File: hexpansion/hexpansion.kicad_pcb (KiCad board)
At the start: 2 copper layers, 32 x 36.6 mm, 17 parts, among them J1 Hexpansion-Connector, J2 Conn_01x08_Pin, U1 24LC00, U2 ATSHA204A-SSHDA

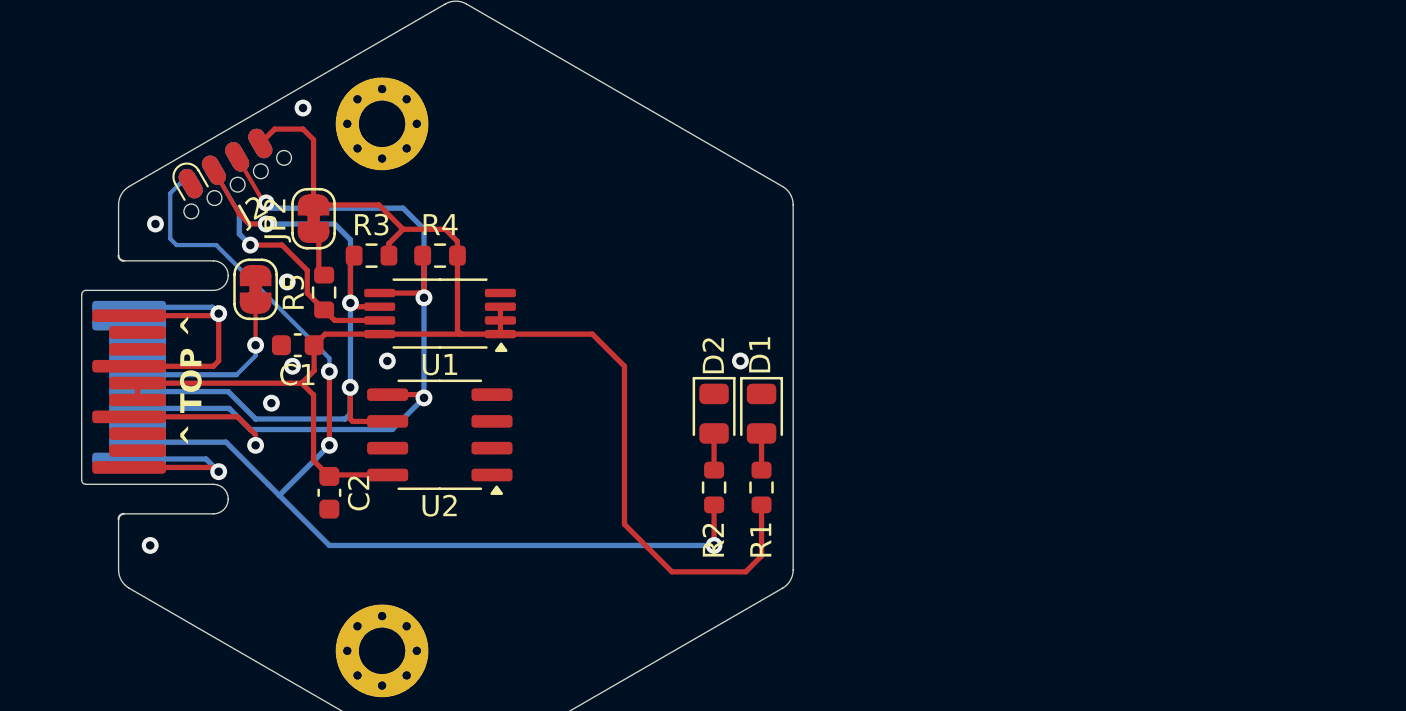
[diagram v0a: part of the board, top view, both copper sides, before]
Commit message: Update hexpansion design
Adds TVS diode
Removes seperate programming connector
tidy up PCB layout
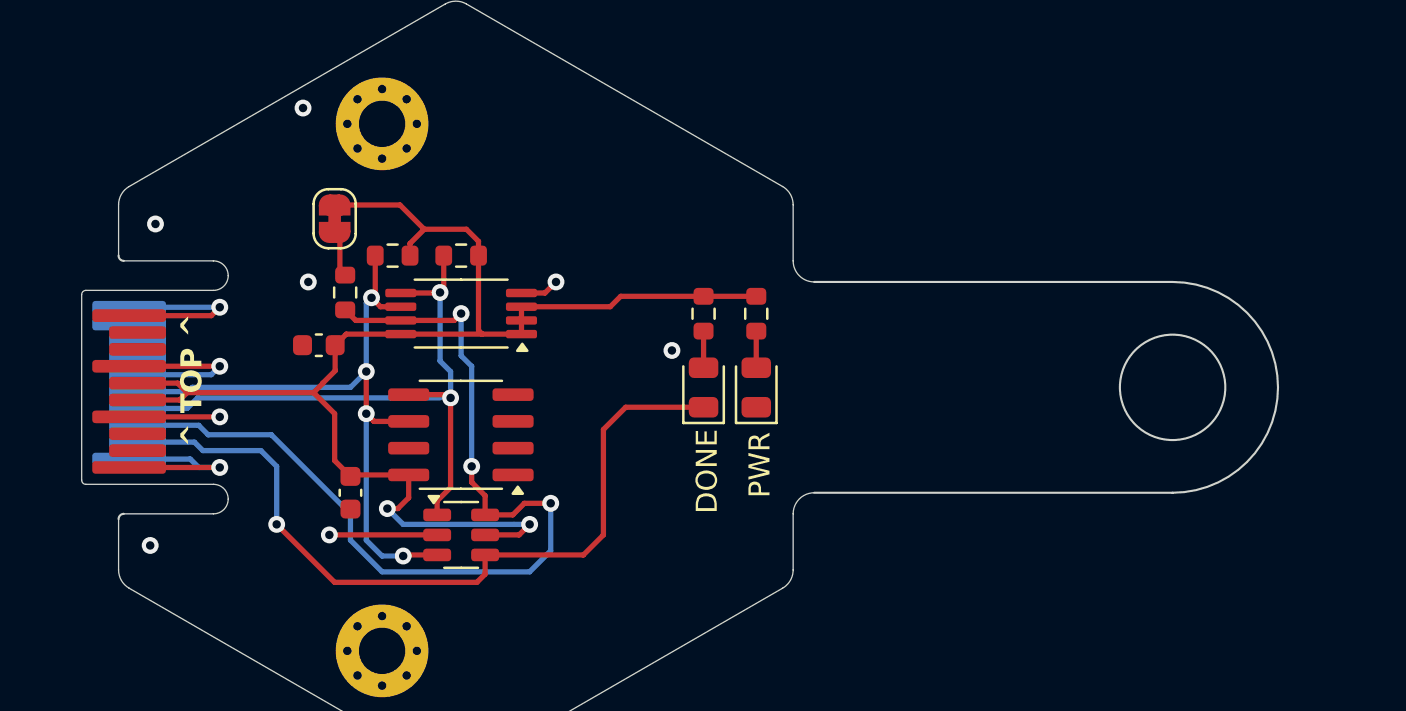
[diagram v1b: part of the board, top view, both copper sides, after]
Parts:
- removed J2: Conn_01x08_Pin, hexpansion:SOIC_clipProgSmall
- removed JP1: SolderJumper_2_Bridged, Jumper:SolderJumper-2_P1.3mm_Bridged_RoundedPad1.0x1.5mm
- added U3: WE-TVS-824015043, Package_TO_SOT_SMD:SOT-23-6, F.Cu at (116.2, 107.0)
- moved R2 8.26 mm to (127.8, 96.5), turned to -90 degrees
- moved R1 8.25 mm to (130.2, 96.5), turned to -90 degrees
- moved D2 1.34 mm to (127.8, 100.0), turned to 90 degrees
- moved D1 1.27 mm to (130.2, 100.0), turned to 90 degrees
- moved C1 1.00 mm to (109.5, 98.0)
- moved C2 1.00 mm to (111.0, 105.0)
- moved JP2 1.00 mm to (110.2, 92.0)
- moved R3 1.00 mm to (113.0, 93.8)
- moved R4 1.00 mm to (116.2, 93.8)
- moved R5 1.00 mm to (110.8, 95.5)
- moved U1 1.00 mm to (116.2, 96.5)
- moved U2 1.00 mm to (116.2, 102.2)
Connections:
- D2 pad 1: GND -> /LED_STATUS
- J1 pad 3: unconnected-(J1-LS_B-Pad3) -> /EEPROM_WP
- J1 pad 6: /HEXP_DET -> GND
- R2 pad 1: /LED_STATUS -> +3V3
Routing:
- net /EEPROM_WP: track 12.3 -> 45.1 mm, vias 1 -> 3
- net /LED_STATUS: track 52.0 -> 38.1 mm, vias 3 -> 1
- net /HEXP_DET: track 8.47 -> 0.00 mm, vias 1 -> 0
- net /SDA: track 38.9 -> 31.3 mm, vias 3 -> 2
- net GND: track 30.5 -> 37.2 mm
- net +3V3: track 72.6 -> 68.1 mm, vias 0 -> 2
- net /SCL: track 34.2 -> 32.3 mm, vias 3 -> 4
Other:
- board size 32 x 36.6 mm -> 55 x 36.6 mm
- board text added: "DONE"
- board text added: "PWR"

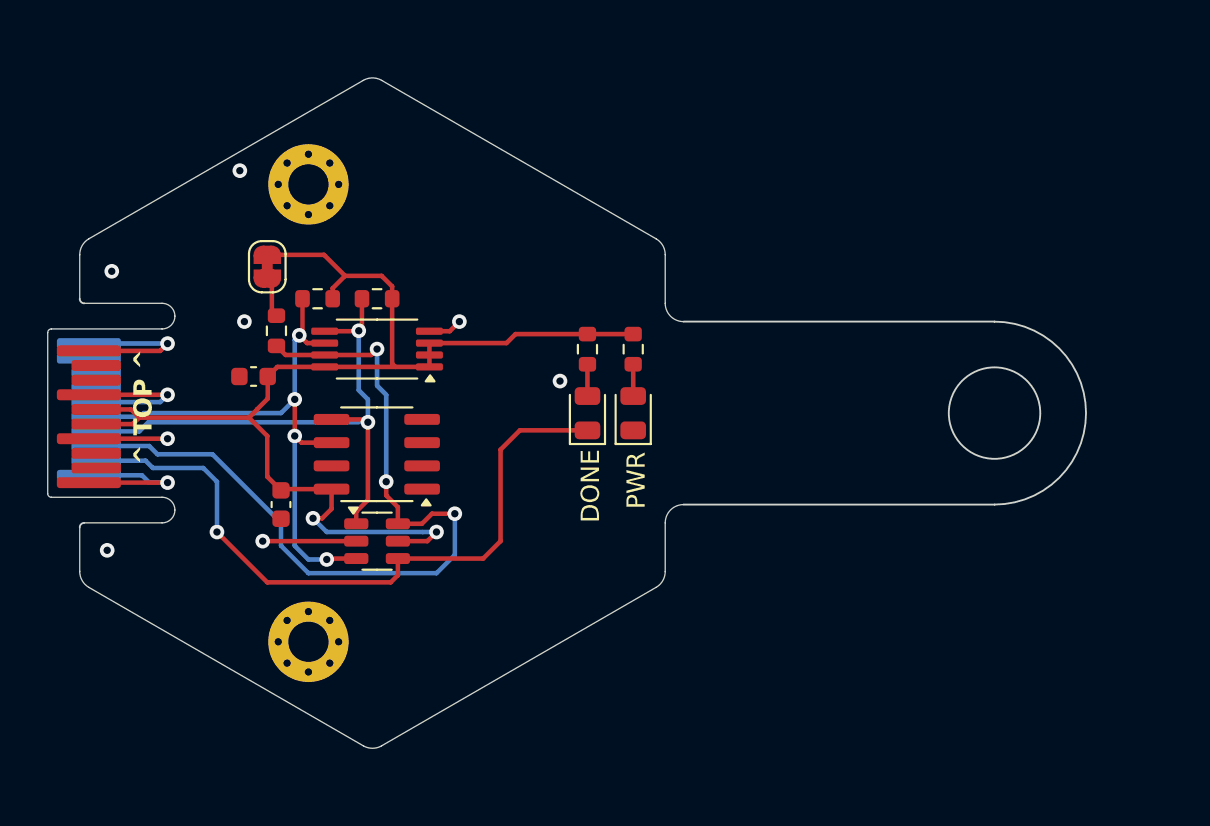
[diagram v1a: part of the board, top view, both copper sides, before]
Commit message: Add pcb arwork and prep for manufacture.
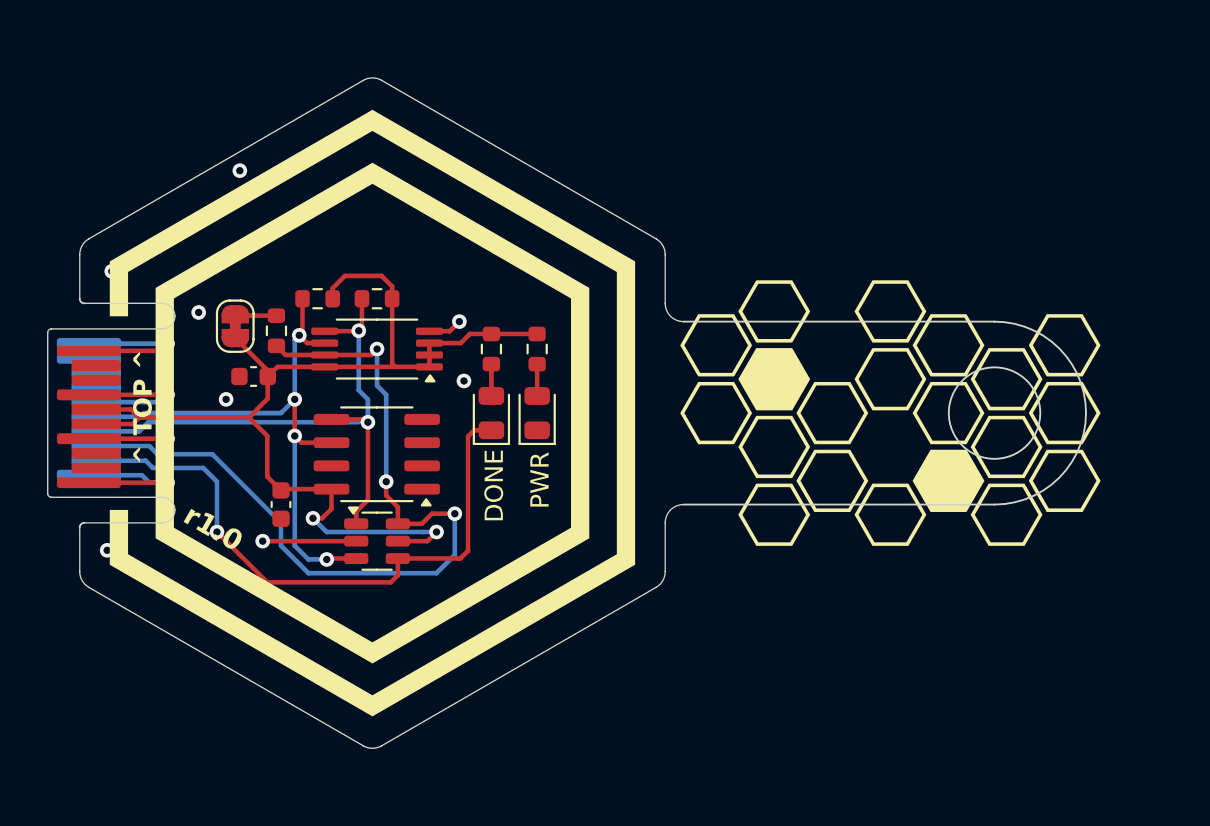
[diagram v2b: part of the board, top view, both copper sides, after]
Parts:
- removed H1, H2: MountingHole_Pad, MountingHole:MountingHole_2.2mm_M2_Pad_Via
- D1: value LED -> NCD0805R1
- D2: value LED -> KT-0805G
- R1: value R -> 75R
- R2: value R -> 33R
- U1: value 24LC00 -> ZD24C64A-XGMT
- U3: value WE-TVS-824015043 -> USBLC6-4SC6
- moved D1 5.25 mm to (125.0, 100.0)
- moved D2 5.25 mm to (122.5, 100.0)
- moved R1 5.25 mm to (125.0, 96.5)
- moved R2 5.25 mm to (122.5, 96.5)
- moved JP2 3.69 mm to (108.5, 95.2), turned to -90 degrees
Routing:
- net +3V3: track 68.1 -> 61.0 mm
- net /LED_STATUS: track 38.1 -> 33.6 mm
- net GND: vias 11 -> 12
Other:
- board text added: "r1.0"
